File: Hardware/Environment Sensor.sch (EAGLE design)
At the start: 8 parts, among them IC1 ATMEGA644A

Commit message: updated component values
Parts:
- C1, C2: value (none) -> 22p
- C3: value (none) -> 0.1u
- Q1: value (none) -> 8MHz
- R2: value (none) -> 10k
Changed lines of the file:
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@@
 <parts>
 <part name="IC1" library="atmel" deviceset="ATMEGA644" device="A"/>
-<part name="Q1" library="crystal" deviceset="CRYSTAL" device="HC49UP"/>
-<part name="C1" library="rcl" deviceset="C-EU" device="C1206K"/>
-<part name="C2" library="rcl" deviceset="C-EU" device="C1206K"/>
+<part name="Q1" library="crystal" deviceset="CRYSTAL" device="HC49UP" value="8MHz"/>
+<part name="C1" library="rcl" deviceset="C-EU" device="C1206K" value="22p"/>
+<part name="C2" library="rcl" deviceset="C-EU" device="C1206K" value="22p"/>
 <part name="P+1" library="supply1" deviceset="VCC" device=""/>
 <part name="GND1" library="supply1" deviceset="GND" device=""/>
@@
 <part name="GND3" library="supply1" deviceset="GND" device=""/>
 <part name="P+2" library="supply1" deviceset="VCC" device=""/>
-<part name="R2" library="rcl" deviceset="R-EU_" device="R1206"/>
+<part name="R2" library="rcl" deviceset="R-EU_" device="R1206" value="10k"/>
 <part name="P+3" library="supply1" deviceset="VCC" device=""/>
 <part name="GND4" library="supply1" deviceset="GND" device=""/>
-<part name="C3" library="rcl" deviceset="C-EU" device="C1206K"/>
+<part name="C3" library="rcl" deviceset="C-EU" device="C1206K" value="0.1u"/>
 </parts>
 <sheets>

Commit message: added analog circuitry
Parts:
- added C4: (no value), rcl:C-EUC1206
- added L1: 10u, rcl:L-EUL3216C
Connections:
- new net N$8: C4.1, IC1.AREF, L1.1
- net GND: now also C4.2
- net VCC: now also IC1.AVCC, L1.2
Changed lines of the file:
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@@
 <part name="GND4" library="supply1" deviceset="GND" device=""/>
 <part name="C3" library="rcl" deviceset="C-EU" device="C1206K" value="0.1u"/>
+<part name="P+4" library="supply1" deviceset="VCC" device=""/>
+<part name="L1" library="rcl" deviceset="L-EU" device="L3216C" value="10u"/>
+<part name="C4" library="rcl" deviceset="C-EU" device="C1206"/>
+<part name="GND5" library="supply1" deviceset="GND" device=""/>
 </parts>
 <sheets>
@@
 <instance part="GND4" gate="1" x="68.58" y="144.78"/>
 <instance part="C3" gate="G$1" x="45.72" y="139.7" rot="R90"/>
+<instance part="P+4" gate="VCC" x="114.3" y="134.62"/>
+<instance part="L1" gate="G$1" x="121.92" y="132.08" rot="R270"/>
+<instance part="C4" gate="G$1" x="124.46" y="124.46"/>
+<instance part="GND5" gate="1" x="124.46" y="114.3"/>
 </instances>
 <busses>
@@
 <wire x1="20.32" y1="149.86" x2="33.02" y2="149.86" width="0.1524" layer="91"/>
 <junction x="33.02" y="149.86"/>
+</segment>
+<segment>
+<wire x1="116.84" y1="132.08" x2="116.84" y2="129.54" width="0.1524" layer="91"/>
+<wire x1="116.84" y1="129.54" x2="114.3" y2="129.54" width="0.1524" layer="91"/>
+<pinref part="P+4" gate="VCC" pin="VCC"/>
+<wire x1="114.3" y1="129.54" x2="114.3" y2="132.08" width="0.1524" layer="91"/>
+<pinref part="IC1" gate="G$1" pin="AVCC"/>
+<wire x1="129.54" y1="132.08" x2="127" y2="129.54" width="0.1524" layer="91"/>
+<wire x1="127" y1="129.54" x2="116.84" y2="129.54" width="0.1524" layer="91"/>
+<junction x="116.84" y="129.54"/>
+<pinref part="L1" gate="G$1" pin="2"/>
 </segment>
 </net>
@@
 <junction x="63.5" y="149.86"/>
 </segment>
+<segment>
+<pinref part="C4" gate="G$1" pin="2"/>
+<pinref part="GND5" gate="1" pin="GND"/>
+<wire x1="124.46" y1="119.38" x2="124.46" y2="116.84" width="0.1524" layer="91"/>
+</segment>
 </net>
 <net name="N$1" class="0">
@@
 <wire x1="109.22" y1="132.08" x2="109.22" y2="129.54" width="0.1524" layer="91"/>
 <pinref part="IC1" gate="G$1" pin="XTAL1"/>
-<wire x1="129.54" y1="139.7" x2="109.22" y2="139.7" width="0.1524" layer="91"/>
 <wire x1="109.22" y1="139.7" x2="109.22" y2="132.08" width="0.1524" layer="91"/>
 <junction x="109.22" y="132.08"/>
+<wire x1="109.22" y1="139.7" x2="129.54" y2="139.7" width="0.1524" layer="91"/>
 </segment>
 </net>
@@
 </segment>
 </net>
+<net name="N$8" class="0">
+<segment>
+<pinref part="C4" gate="G$1" pin="1"/>
+<wire x1="124.46" y1="127" x2="111.76" y2="127" width="0.1524" layer="91"/>
+<wire x1="111.76" y1="127" x2="111.76" y2="137.16" width="0.1524" layer="91"/>
+<wire x1="111.76" y1="137.16" x2="127" y2="137.16" width="0.1524" layer="91"/>
+<pinref part="IC1" gate="G$1" pin="AREF"/>
+<pinref part="L1" gate="G$1" pin="1"/>
+<wire x1="127" y1="132.08" x2="129.54" y2="134.62" width="0.1524" layer="91"/>
+<wire x1="127" y1="137.16" x2="127" y2="132.08" width="0.1524" layer="91"/>
+<junction x="127" y="132.08"/>
+</segment>
+</net>

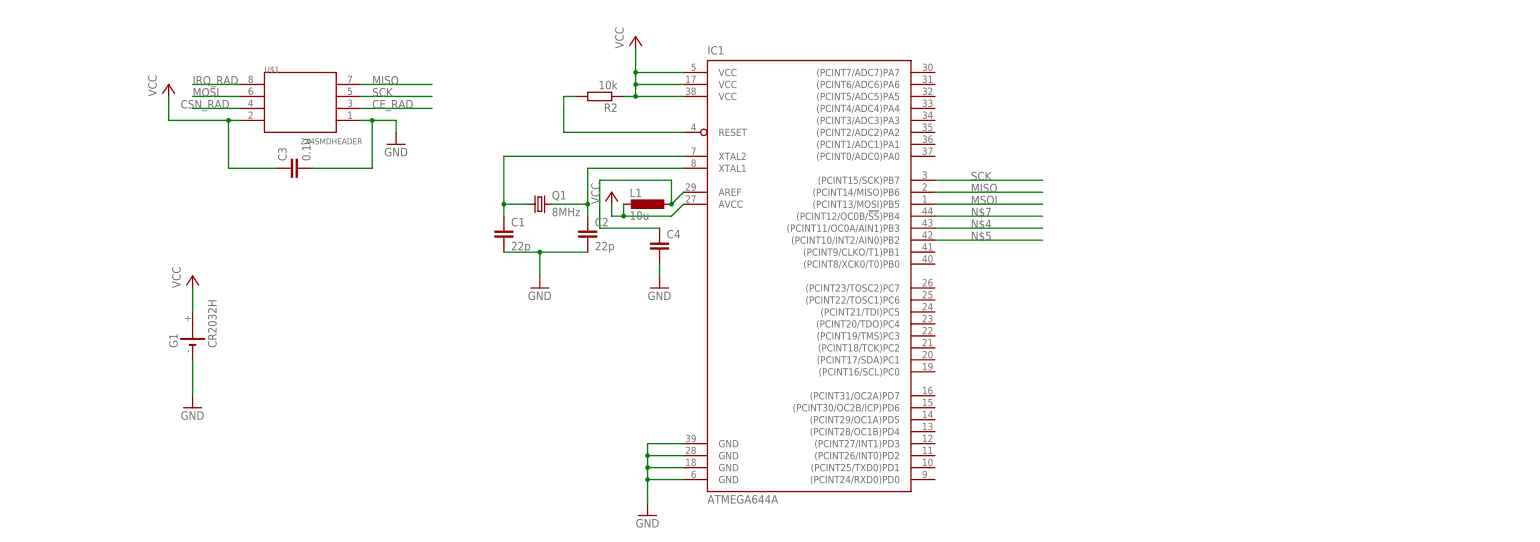
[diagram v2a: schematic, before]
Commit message: created library parts for : Si7006-A20 ATMEGA328P-AU (TQFP32) APDS AMBIENT LIGHT SENSOR
Updated Environment sensor with up to date schematic
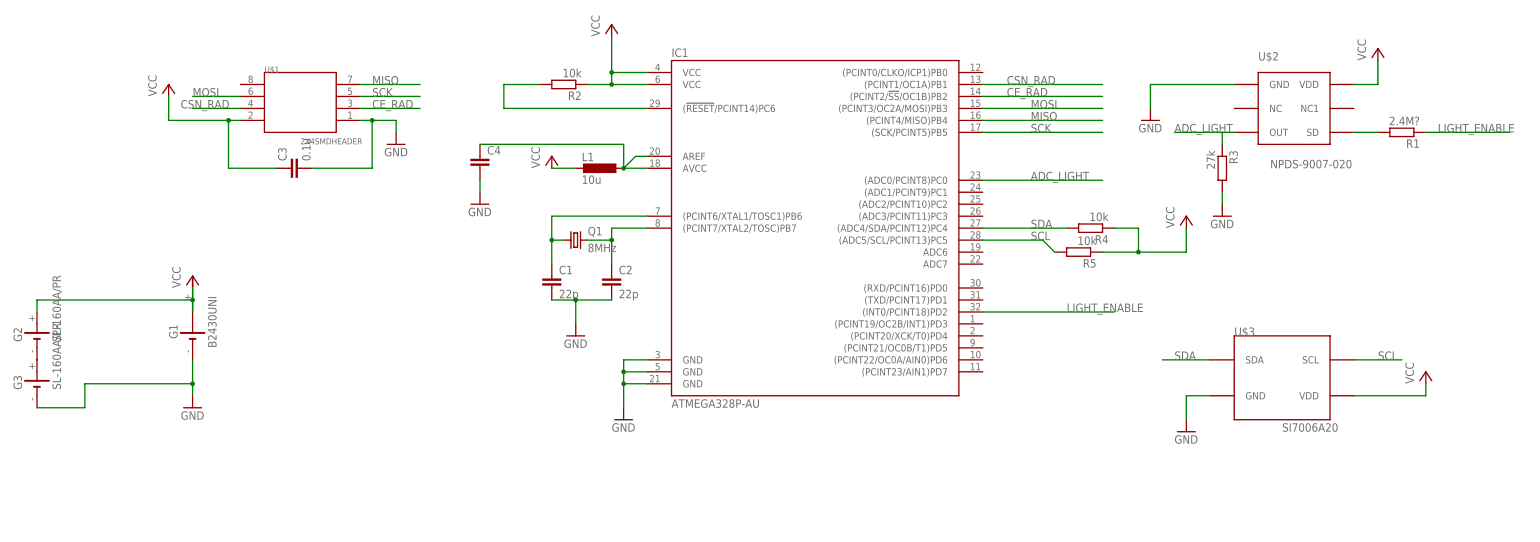
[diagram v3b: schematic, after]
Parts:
- added G2, G3: SL-160AA/PR, battery:SL-160AA/PR
- added R1: 2.4M?, rcl:R-EU_R1206
- added R3: 27k, rcl:R-EU_R1206
- added R4, R5: 10k, rcl:R-EU_R1206
- added U$2: NPDS-9007-020, APDS:NPDS-9007-020
- added U$3: SI7006A20, Si7006:SI7006A20
- G1: value CR2032H -> B2430UNI; device battery:CR2032H -> battery:B2430UNI
- IC1: value ATMEGA644A -> ATMEGA328P-AU; device atmel:ATMEGA644A -> ATMEGA328P:ATMEGA328P-AU
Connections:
- removed net IRQ_RAD: U$1.8
- removed net MSOI: IC1.(PCINT13/MOSI)PB5
- removed net N$7: IC1.(PCINT12/OC0B/!SS!)PB4
- new net ADC_LIGHT: IC1.(ADC0/PCINT8)PC0, R3.1, U$2.OUT
- new net LIGHT_ENABLE: IC1.(INT0/PCINT18)PD2, R1.1
- new net SCL: IC1.(ADC5/SCL/PCINT13)PC5, R5.2, U$3.SCL
- new net SDA: IC1.(ADC4/SDA/PCINT12)PC4, R4.2, U$3.SDA
- net CE_RAD: now also IC1.(PCINT2/!SS!/OC1B)PB2
- net CSN_RAD: now also IC1.(PCINT1/OC1A)PB1
- net GND: now also G3.-, R3.2, U$2.GND, U$3.GND; no longer IC1.GND@3
- net MISO: now also IC1.(PCINT4/MISO)PB4; no longer IC1.(PCINT14/MISO)PB6
- net MOSI: now also IC1.(PCINT3/OC2A/MOSI)PB3
- net N$1: now also IC1.(PCINT6/XTAL1/TOSC1)PB6; no longer IC1.XTAL2
- net N$2: now also IC1.(PCINT7/XTAL2/TOSC)PB7; no longer IC1.XTAL1
- net N$3: now also IC1.(!RESET!/PCINT14)PC6; no longer IC1.RESET
- net N$4: now also G2.-, G3.+; no longer IC1.(PCINT11/OC0A/AIN1)PB3
- net N$5: now also R1.2, U$2.SD; no longer IC1.(PCINT10/INT2/AIN0)PB2
- net N$8: now also IC1.AVCC
- net SCK: now also IC1.(SCK/PCINT5)PB5; no longer IC1.(PCINT15/SCK)PB7
- net VCC: now also G1.+@2, G1.+@3, G2.+, R4.1, R5.1, U$2.VDD, U$3.VDD; no longer G1.+, IC1.AVCC, IC1.VCC@2
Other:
- moved on the sheet: C1, C2, C4, L1, Q1, R2

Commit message: created mock up of Board
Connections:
- net VCC: now also G1.+, G1.+@1, G1.+@4
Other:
- moved on the sheet: G1
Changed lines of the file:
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@@
 <instance part="U$1" gate="G$1" x="48.26" y="154.94"/>
 <instance part="GND2" gate="1" x="106.68" y="104.14"/>
-<instance part="G1" gate="G$1" x="25.4" y="104.14" rot="R90"/>
+<instance part="G1" gate="G$1" x="35.56" y="104.14" rot="R90"/>
 <instance part="GND3" gate="1" x="25.4" y="88.9"/>
-<instance part="P+2" gate="VCC" x="25.4" y="116.84"/>
+<instance part="P+2" gate="VCC" x="30.48" y="119.38"/>
 <instance part="R2" gate="G$1" x="104.14" y="157.48" rot="R180"/>
 <instance part="P+3" gate="VCC" x="20.32" y="157.48"/>
@@
 </segment>
 <segment>
+<pinref part="P+2" gate="VCC" pin="VCC"/>
+<pinref part="G2" gate="G$1" pin="+"/>
+<wire x1="35.56" y1="111.76" x2="30.48" y2="116.84" width="0.1524" layer="91"/>
+<wire x1="-7.62" y1="109.22" x2="-7.62" y2="111.76" width="0.1524" layer="91"/>
+<wire x1="-7.62" y1="111.76" x2="35.56" y2="111.76" width="0.1524" layer="91"/>
+<pinref part="G1" gate="G$1" pin="+@2"/>
+<junction x="35.56" y="111.76"/>
+<pinref part="G1" gate="G$1" pin="+"/>
+<wire x1="35.56" y1="116.84" x2="40.64" y2="116.84" width="0.1524" layer="91"/>
+<wire x1="40.64" y1="116.84" x2="40.64" y2="114.3" width="0.1524" layer="91"/>
+<wire x1="40.64" y1="114.3" x2="40.64" y2="111.76" width="0.1524" layer="91"/>
+<wire x1="40.64" y1="111.76" x2="35.56" y2="111.76" width="0.1524" layer="91"/>
 <pinref part="G1" gate="G$1" pin="+@3"/>
-<pinref part="P+2" gate="VCC" pin="VCC"/>
-<wire x1="25.4" y1="109.22" x2="25.4" y2="111.76" width="0.1524" layer="91"/>
-<pinref part="G2" gate="G$1" pin="+"/>
-<wire x1="25.4" y1="111.76" x2="25.4" y2="114.3" width="0.1524" layer="91"/>
-<wire x1="-7.62" y1="109.22" x2="-7.62" y2="111.76" width="0.1524" layer="91"/>
-<wire x1="-7.62" y1="111.76" x2="25.4" y2="111.76" width="0.1524" layer="91"/>
-<pinref part="G1" gate="G$1" pin="+@2"/>
-<junction x="25.4" y="111.76"/>
+<wire x1="35.56" y1="109.22" x2="40.64" y2="109.22" width="0.1524" layer="91"/>
+<wire x1="40.64" y1="109.22" x2="40.64" y2="111.76" width="0.1524" layer="91"/>
+<junction x="40.64" y="111.76"/>
+<pinref part="G1" gate="G$1" pin="+@4"/>
+<wire x1="35.56" y1="106.68" x2="40.64" y2="106.68" width="0.1524" layer="91"/>
+<wire x1="40.64" y1="106.68" x2="40.64" y2="109.22" width="0.1524" layer="91"/>
+<junction x="40.64" y="109.22"/>
+<pinref part="G1" gate="G$1" pin="+@1"/>
+<wire x1="35.56" y1="114.3" x2="40.64" y2="114.3" width="0.1524" layer="91"/>
+<junction x="40.64" y="114.3"/>
 </segment>
 <segment>
@@
 <pinref part="G1" gate="G$1" pin="-"/>
 <pinref part="GND3" gate="1" pin="GND"/>
-<wire x1="25.4" y1="99.06" x2="25.4" y2="93.98" width="0.1524" layer="91"/>
+<wire x1="35.56" y1="99.06" x2="25.4" y2="93.98" width="0.1524" layer="91"/>
 <pinref part="G3" gate="G$1" pin="-"/>
 <wire x1="25.4" y1="93.98" x2="25.4" y2="91.44" width="0.1524" layer="91"/>
@@
 <wire x1="243.84" y1="147.32" x2="233.68" y2="147.32" width="0.1524" layer="91"/>
 <wire x1="243.84" y1="144.78" x2="243.84" y2="147.32" width="0.1524" layer="91"/>
-</segment>
-</net>
+<junction x="243.84" y="147.32"/>
+</segment>
+</net>
